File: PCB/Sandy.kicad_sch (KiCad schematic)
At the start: 241 parts, among them J1 USB_C_Receptacle_USB2.0, J10 Conn_01x08, J11 Conn_01x08, J12 Conn_01x08, J13 Conn_01x08, J14 Conn_01x08, J15 Conn_01x08, J16 Conn_01x04, J17 Conn_01x04, J18 Conn_01x04, J19 Conn_01x04, J2 Conn_01x03, J20 Conn_01x04, J21 Conn_01x04, J22 Conn_01x04, J23 Conn_01x04, J24 Conn_01x04, J25 Conn_01x04, J26 Conn_01x04, J27 Conn_01x04, J28 Conn_01x04, J29 Conn_01x04, J3 Conn_01x02, J30 Conn_01x04, J31 Conn_01x04, J5 Conn_02x03_Odd_Even, J8 Conn_01x08, J9 Conn_01x08, U1 ATmega32U4-MU, U2 24LC64, Y1 16MHz

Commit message: ミドルとトップをシート分割
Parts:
- removed #J10, #J11, #J12, #J13, #J14, #J9: Conn_02x04_Row_Letter_Last, symbol Connector_Generic:Conn_02x04_Row_Letter_Last
- removed D12, D13, D14, D15, D16, D17, D18, D19, D21, D23, D25, D26, D29, D30, D31, D33, D36, D61, D62, D63, D64, D65, D67, D68, D69, D71, D73, D75, D78, D83, D85, D95: D, Diode_SMD:D_SOD-123, symbol Device:D
- removed J10, J11, J12, J13, J14, J15, J8, J9: Conn_01x08, symbol Connector_Generic:Conn_01x08
- removed J17, J19, J20, J21, J22, J23, J24, J25, J26, J27, J28, J29, J30, J31: Conn_01x04, symbol Connector_Generic:Conn_01x04
- removed SW_'1, SW_-1, SW_0, SW_1, SW_2, SW_3, SW_4, SW_5, SW_6, SW_7, SW_8, SW_9, SW_;3, SW_=1, SW_B1, SW_B2, SW_Center1, SW_ESC1, SW_G1, SW_H1, SW_P1, SW_Q1, SW_R1, SW_T1, SW_U1, SW_Y1, SW_[1, SW_\1, SW_]1, SW_`1: SW_Push, MX_Alps_Hybrid:MXOnly-1U-Hotswap-guide, symbol Switch:SW_Push
- removed SW_;2: SW_Push, MX_Alps_Hybrid:MXOnly-1U-NoLED, symbol Switch:SW_Push
- removed SW_BS1.5u1, SW_TAB1.25u1, SW_TAB1.5u1: SW_Push, MX_Alps_Hybrid:MXOnly-1.5U-Hotswap-guide, symbol Switch:SW_Push
- added J4, J6, J7, J8: Conn_02x04_Top_Bottom, symbol Connector_Generic:Conn_02x04_Top_Bottom
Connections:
- net MISO: now also J4.8 (Pin_8), J6.8 (Pin_8)
- net MOSI: now also J4.7 (Pin_7), J6.7 (Pin_7)
- net Mid_row2: now also #J6.1b (Pin_1b)
- net Mid_row3: now also #J8.1b (Pin_1b)
- net Mid_row7: now also #J6.2b (Pin_2b)
- net Mid_row8: now also #J8.2b (Pin_2b)
- net RE_L1_1: now also J4.5 (Pin_5), J6.5 (Pin_5)
- net RE_R1_1: now also J7.8 (Pin_8), J8.8 (Pin_8)
- net RE_R2_1: now also J7.5 (Pin_5), J8.5 (Pin_5)
- net SCK: now also J4.6 (Pin_6), J6.6 (Pin_6)
- net col5: now also J7.6 (Pin_6), J8.6 (Pin_6)
- net col6: now also J7.7 (Pin_7), J8.7 (Pin_7)
- net row0: now also J4.1 (Pin_1), J6.1 (Pin_1)
- net row1: now also J4.3 (Pin_3), J6.3 (Pin_3)
- net row2: now also #J6.1a (Pin_1a), J16.1 (Pin_1), J7.1 (Pin_1), J8.1 (Pin_1)
- net row3: now also #J8.1a (Pin_1a), J18.1 (Pin_1), J7.3 (Pin_3), J8.3 (Pin_3)
- net row4: no longer #J6.1a (Pin_1a), #J8.1a (Pin_1a), J16.1 (Pin_1), J18.1 (Pin_1)
- net row5: now also J4.2 (Pin_2), J6.2 (Pin_2)
- net row6: now also J4.4 (Pin_4), J6.4 (Pin_4)
- net row7: now also #J6.2a (Pin_2a), J16.2 (Pin_2), J7.2 (Pin_2), J8.2 (Pin_2)
- net row8: now also #J8.2a (Pin_2a), J18.2 (Pin_2), J7.4 (Pin_4), J8.4 (Pin_4)
- net row9: no longer #J6.2a (Pin_2a), #J8.2a (Pin_2a), J16.2 (Pin_2), J18.2 (Pin_2)
- removed net Mid_row4: #J6.1b (Pin_1b), #J8.1b (Pin_1b)
- removed net Mid_row9: #J6.2b (Pin_2b), #J8.2b (Pin_2b)
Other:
- added sheet matrix_middle (matrix_middle.kicad_sch)
- added sheet matrix_top (matrix_top.kicad_sch)
- note added: "Virtual Connection"
- note removed: "Panel CONNECTOR Middle to Top"

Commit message: MCUさっくり配置
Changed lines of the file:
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@@
     (stroke (width 0.1524) (type solid) (color 0 0 0 0))
     (fill (color 0 0 0 0.0000))
-    (property "Sheet name" "matrix_middle" (id 0) (at 80.01 17.0684 0)
-      (effects (font (size 1.27 1.27)) (justify left bottom))
+    (property "Sheet name" "matrix_middle" (id 0) (at 80.01 16.4334 0)
+      (effects (font (size 2.54 2.54) bold) (justify left bottom))
     )
     (property "Sheet file" "matrix_middle.kicad_sch" (id 1) (at 80.01 25.9846 0)
@@
     (stroke (width 0.1524) (type solid) (color 0 0 0 0))
     (fill (color 0 0 0 0.0000))
-    (property "Sheet name" "matrix_top" (id 0) (at 128.27 17.0684 0)
-      (effects (font (size 1.27 1.27)) (justify left bottom))
+    (property "Sheet name" "matrix_top" (id 0) (at 128.27 16.4334 0)
+      (effects (font (size 2.54 2.54) bold) (justify left bottom))
     )
     (property "Sheet file" "matrix_top.kicad_sch" (id 1) (at 128.27 25.9846 0)

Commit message: レイアウト調整
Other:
- moved on the sheet: C1, C2, C3, C4, C5, C6, C7, D10, D11, D22, D24, D27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

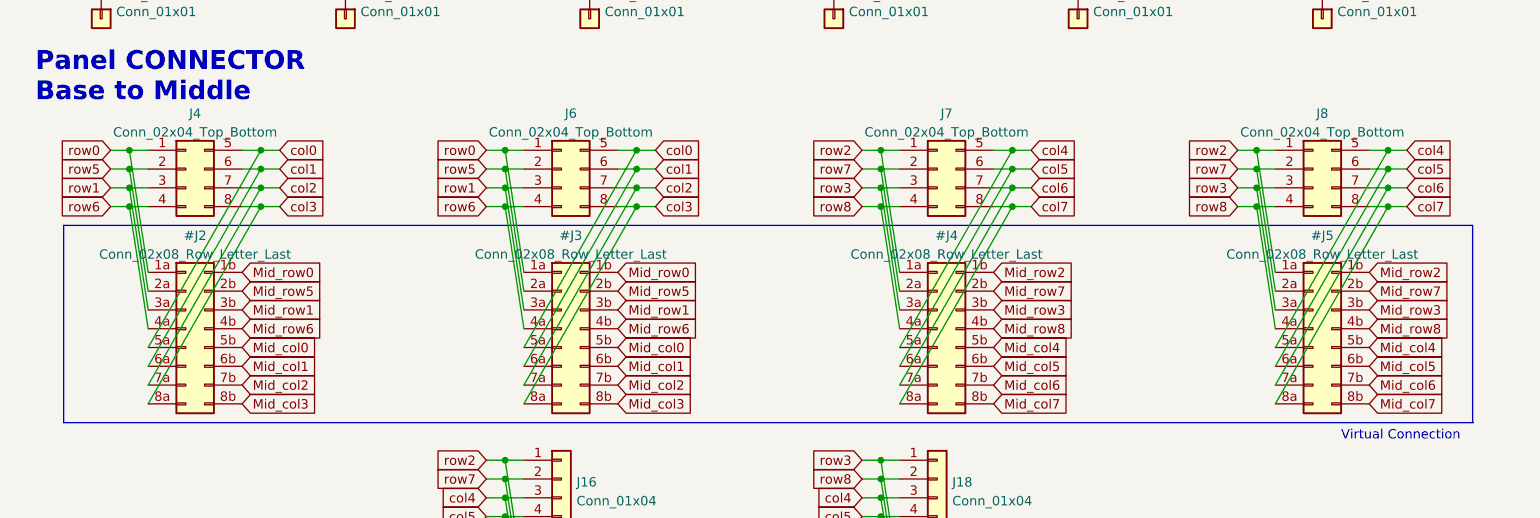
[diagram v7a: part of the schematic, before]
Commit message: ピンヘッダのピン順を変更。フットプリント割り当て。
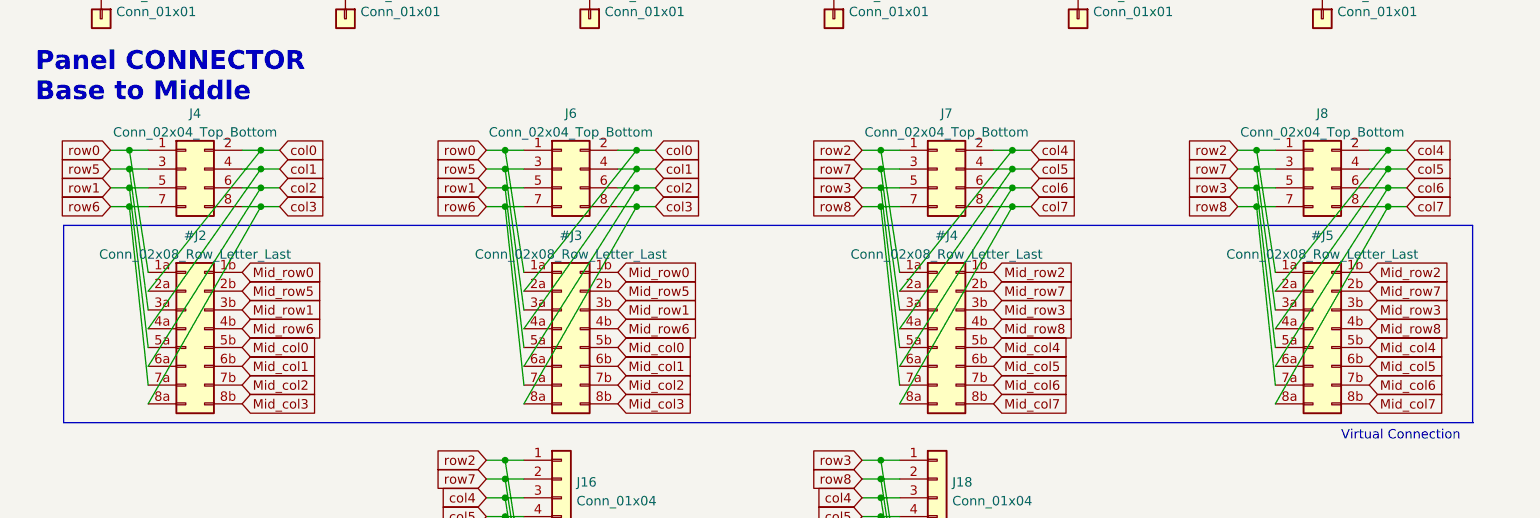
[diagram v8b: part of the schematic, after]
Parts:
- EXT_C0, EXT_C1, EXT_C2, EXT_C3, EXT_C4, EXT_C5, EXT_C6, EXT_C7, EXT_R0, EXT_R1, EXT_R2, EXT_R3, EXT_R4, EXT_R5, EXT_R6, EXT_R7, EXT_R8, EXT_R9: footprint TestPoint:TestPoint_THTPad_D1.5mm_Drill0.7mm -> TestPoint:TestPoint_THTPad_D2.0mm_Drill1.0mm
- J16, J18: footprint (none) -> Connector_PinHeader_2.54mm:PinHeader_1x04_P2.54mm_Vertical
- J4, J6, J7, J8: footprint (none) -> Connector_PinHeader_2.54mm:PinHeader_2x04_P2.54mm_Vertical; symbol Connector_Generic:Conn_02x04_Top_Bottom -> Connector_Generic:Conn_02x04_Odd_Even
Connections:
- net MOSI: now also #J2.6a (Pin_6a), #J3.6a (Pin_6a), J4.6 (Pin_6), J6.6 (Pin_6); no longer #J2.7a (Pin_7a), #J3.7a (Pin_7a), J4.7 (Pin_7), J6.7 (Pin_7)
- net RE_L1_1: now also #J2.2a (Pin_2a), #J3.2a (Pin_2a), J4.2 (Pin_2), J6.2 (Pin_2); no longer #J2.5a (Pin_5a), #J3.5a (Pin_5a), J4.5 (Pin_5), J6.5 (Pin_5)
- net RE_R2_1: now also #J4.2a (Pin_2a), #J5.2a (Pin_2a), J7.2 (Pin_2), J8.2 (Pin_2); no longer #J4.5a (Pin_5a), #J5.5a (Pin_5a), J7.5 (Pin_5), J8.5 (Pin_5)
- net SCK: now also #J2.4a (Pin_4a), #J3.4a (Pin_4a), J4.4 (Pin_4), J6.4 (Pin_4); no longer #J2.6a (Pin_6a), #J3.6a (Pin_6a), J4.6 (Pin_6), J6.6 (Pin_6)
- net col5: now also #J4.4a (Pin_4a), #J5.4a (Pin_4a), J7.4 (Pin_4), J8.4 (Pin_4); no longer #J4.6a (Pin_6a), #J5.6a (Pin_6a), J7.6 (Pin_6), J8.6 (Pin_6)
- net col6: now also #J4.6a (Pin_6a), #J5.6a (Pin_6a), J7.6 (Pin_6), J8.6 (Pin_6); no longer #J4.7a (Pin_7a), #J5.7a (Pin_7a), J7.7 (Pin_7), J8.7 (Pin_7)
- net row1: now also #J2.5a (Pin_5a), #J3.5a (Pin_5a), J4.5 (Pin_5), J6.5 (Pin_5); no longer #J2.3a (Pin_3a), #J3.3a (Pin_3a), J4.3 (Pin_3), J6.3 (Pin_3)
- net row3: now also #J4.5a (Pin_5a), #J5.5a (Pin_5a), J7.5 (Pin_5), J8.5 (Pin_5); no longer #J4.3a (Pin_3a), #J5.3a (Pin_3a), J7.3 (Pin_3), J8.3 (Pin_3)
- net row5: now also #J2.3a (Pin_3a), #J3.3a (Pin_3a), J4.3 (Pin_3), J6.3 (Pin_3); no longer #J2.2a (Pin_2a), #J3.2a (Pin_2a), J4.2 (Pin_2), J6.2 (Pin_2)
- net row6: now also #J2.7a (Pin_7a), #J3.7a (Pin_7a), J4.7 (Pin_7), J6.7 (Pin_7); no longer #J2.4a (Pin_4a), #J3.4a (Pin_4a), J4.4 (Pin_4), J6.4 (Pin_4)
- net row7: now also #J4.3a (Pin_3a), #J5.3a (Pin_3a), J7.3 (Pin_3), J8.3 (Pin_3); no longer #J4.2a (Pin_2a), #J5.2a (Pin_2a), J7.2 (Pin_2), J8.2 (Pin_2)
- net row8: now also #J4.7a (Pin_7a), #J5.7a (Pin_7a), J7.7 (Pin_7), J8.7 (Pin_7); no longer #J4.4a (Pin_4a), #J5.4a (Pin_4a), J7.4 (Pin_4), J8.4 (Pin_4)
